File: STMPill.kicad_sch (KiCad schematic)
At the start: 65 parts, among them J1 Conn_Coaxial, J2 TC2030, J3 USB_C_16P, J4 Conn_01x20_L, J5 Conn_01x20_R, Q1 SS8550, Q3 SS8050, SW1 SW_Push, SW2 SW_Push, U1 STM32WB55REVx, U2 CP2102N-Axx-xQFN24, U3 TPS78233DDC, U4 USBLC6-2SC6, X1 32MHz, Y1 32.768kHz

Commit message: saving
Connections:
- net +3.3V: now also J4.2 (Pin_2)
- net GND: now also J4.4 (Pin_4); no longer J4.2 (Pin_2)
- net PB5: no longer J4.7 (Pin_7)
- net PB7: now also J4.7 (Pin_7)
- net PC12: no longer J4.4 (Pin_4)
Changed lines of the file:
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@@
 	(wire
 		(pts
+			(xy 33.02 198.12) (xy 38.1 198.12)
+		)
+		(stroke
+			(width 0)
+			(type default)
+		)
+	)
+	(wire
+		(pts
 			(xy 368.3 129.54) (xy 368.3 127)
 		)
@@
 		)
 	)
-	(label "PC12"
-		(at 38.1 198.12 180)
-		(effects
-			(font
-				(size 1.27 1.27)
-			)
-			(justify right bottom)
-		)
-	)
 	(label "PA11"
 		(at 69.85 205.74 180)
@@
 		)
 	)
-	(label "PB5"
+	(label "PB7"
 		(at 38.1 205.74 180)
 		(effects
@@
 	)
 	(symbol
+		(lib_id "power:+3.3V")
+		(at 33.02 193.04 90)
+		(unit 1)
+		(body_style 1)
+		(exclude_from_sim no)
+		(in_bom yes)
+		(on_board yes)
+		(in_pos_files yes)
+		(dnp no)
+		(fields_autoplaced yes)
+		(property "Reference" "#PWR036"
+			(at 36.83 193.04 0)
+			(hide yes)
+			(show_name no)
+			(do_not_autoplace no)
+			(effects
+				(font
+					(size 1.27 1.27)
+				)
+			)
+		)
+		(property "Value" "+3.3V"
+			(at 29.21 193.0399 90)
+			(show_name no)
+			(do_not_autoplace no)
+			(effects
+				(font
+					(size 1.27 1.27)
+				)
+				(justify left)
+			)
+		)
+		(property "Footprint" ""
+			(at 33.02 193.04 0)
+			(hide yes)
+			(show_name no)
+			(do_not_autoplace no)
+			(effects
+				(font
+					(size 1.27 1.27)
+				)
+			)
+		)
+		(property "Datasheet" ""
+			(at 33.02 193.04 0)
+			(hide yes)
+			(show_name no)
+			(do_not_autoplace no)
+			(effects
+				(font
+					(size 1.27 1.27)
+				)
+			)
+		)
+		(property "Description" "Power symbol creates a global label with name \"+3.3V\""
+			(at 33.02 193.04 0)
+			(hide yes)
+			(show_name no)
+			(do_not_autoplace no)
+			(effects
+				(font
+					(size 1.27 1.27)
+				)
+			)
+		)
+		(pin "1"
+		)
+		(instances
+			(project "STMPill"
+				(path "/456d5bce-2783-4e9b-b1a6-9e254196200d"
+					(reference "#PWR036")
+					(unit 1)
+				)
+			)
+		)
+	)
+	(symbol
 		(lib_id "Connector_Generic:Conn_01x20")
 		(at 74.93 213.36 0)
@@
 	)
 	(symbol
+		(lib_id "power:GND")
+		(at 33.02 198.12 270)
+		(unit 1)
+		(body_style 1)
+		(exclude_from_sim no)
+		(in_bom yes)
+		(on_board yes)
+		(in_pos_files yes)
+		(dnp no)
+		(fields_autoplaced yes)
+		(property "Reference" "#PWR037"
+			(at 26.67 198.12 0)
+			(hide yes)
+			(show_name no)
+			(do_not_autoplace no)
+			(effects
+				(font
+					(size 1.27 1.27)
+				)
+			)
+		)
+		(property "Value" "GND"
+			(at 27.94 198.12 0)
+			(hide yes)
+			(show_name no)
+			(do_not_autoplace no)
+			(effects
+				(font
+					(size 1.27 1.27)
+				)
+			)
+		)
+		(property "Footprint" ""
+			(at 33.02 198.12 0)
+			(hide yes)
+			(show_name no)
+			(do_not_autoplace no)
+			(effects
+				(font
+					(size 1.27 1.27)
+				)
+			)
+		)
+		(property "Datasheet" ""
+			(at 33.02 198.12 0)
+			(hide yes)
+			(show_name no)
+			(do_not_autoplace no)
+			(effects
+				(font
+					(size 1.27 1.27)
+				)
+			)
+		)
+		(property "Description" "Power symbol creates a global label with name \"GND\" , ground"
+			(at 33.02 198.12 0)
+			(hide yes)
+			(show_name no)
+			(do_not_autoplace no)
+			(effects
+				(font
+					(size 1.27 1.27)
+				)
+			)
+		)
+		(pin "1"
+		)
+		(instances
+			(project "STMPill"
+				(path "/456d5bce-2783-4e9b-b1a6-9e254196200d"
+					(reference "#PWR037")
+					(unit 1)
+				)
+			)
+		)
+	)
+	(symbol
 		(lib_id "Device:LED")
 		(at 297.18 129.54 90)
@@
 	)
 	(symbol
+		(lib_id "power:GND")
+		(at 33.02 195.58 270)
+		(unit 1)
+		(body_style 1)
+		(exclude_from_sim no)
+		(in_bom yes)
+		(on_board yes)
+		(in_pos_files yes)
+		(dnp no)
+		(fields_autoplaced yes)
+		(property "Reference" "#PWR038"
+			(at 26.67 195.58 0)
+			(hide yes)
+			(show_name no)
+			(do_not_autoplace no)
+			(effects
+				(font
+					(size 1.27 1.27)
+				)
+			)
+		)
+		(property "Value" "GND"
+			(at 27.94 195.58 0)
+			(hide yes)
+			(show_name no)
+			(do_not_autoplace no)
+			(effects
+				(font
+					(size 1.27 1.27)
+				)
+			)
+		)
+		(property "Footprint" ""
+			(at 33.02 195.58 0)
+			(hide yes)
+			(show_name no)
+			(do_not_autoplace no)
+			(effects
+				(font
+					(size 1.27 1.27)
+				)
+			)
+		)
+		(property "Datasheet" ""
+			(at 33.02 195.58 0)
+			(hide yes)
+			(show_name no)
+			(do_not_autoplace no)
+			(effects
+				(font
+					(size 1.27 1.27)
+				)
+			)
+		)
+		(property "Description" "Power symbol creates a global label with name \"GND\" , ground"
+			(at 33.02 195.58 0)
+			(hide yes)
+			(show_name no)
+			(do_not_autoplace no)
+			(effects
+				(font
+					(size 1.27 1.27)
+				)
+			)
+		)
+		(pin "1"
+		)
+		(instances
+			(project "STMPill"
+				(path "/456d5bce-2783-4e9b-b1a6-9e254196200d"
+					(reference "#PWR038")
+					(unit 1)
+				)
+			)
+		)
+	)
+	(symbol
 		(lib_id "Device:C")
 		(at 93.98 41.91 0)
@@
 	(symbol
 		(lib_id "power:GND")
-		(at 33.02 193.04 270)
-		(unit 1)
-		(body_style 1)
-		(exclude_from_sim no)
-		(in_bom yes)
-		(on_board yes)
-		(in_pos_files yes)
-		(dnp no)
-		(fields_autoplaced yes)
-		(property "Reference" "#PWR036"
-			(at 26.67 193.04 0)
-			(hide yes)
-			(show_name no)
-			(do_not_autoplace no)
-			(effects
-				(font
-					(size 1.27 1.27)
-				)
-			)
-		)
-		(property "Value" "GND"
-			(at 27.94 193.04 0)
-			(hide yes)
-			(show_name no)
-			(do_not_autoplace no)
-			(effects
-				(font
-					(size 1.27 1.27)
-				)
-			)
-		)
-		(property "Footprint" ""
-			(at 33.02 193.04 0)
-			(hide yes)
-			(show_name no)
-			(do_not_autoplace no)
-			(effects
-				(font
-					(size 1.27 1.27)
-				)
-			)
-		)
-		(property "Datasheet" ""
-			(at 33.02 193.04 0)
-			(hide yes)
-			(show_name no)
-			(do_not_autoplace no)
-			(effects
-				(font
-					(size 1.27 1.27)
-				)
-			)
-		)
-		(property "Description" "Power symbol creates a global label with name \"GND\" , ground"
-			(at 33.02 193.04 0)
-			(hide yes)
-			(show_name no)
-			(do_not_autoplace no)
-			(effects
-				(font
-					(size 1.27 1.27)
-				)
-			)
-		)
-		(pin "1"
-		)
-		(instances
-			(project "STMPill"
-				(path "/456d5bce-2783-4e9b-b1a6-9e254196200d"
-					(reference "#PWR036")
-					(unit 1)
-				)
-			)
-		)
-	)
-	(symbol
-		(lib_id "power:GND")
 		(at 58.42 193.04 270)
 		(unit 1)
@@
 					(unit 1)
 				)
-			)
-		)
-	)
-	(symbol
-		(lib_id "power:GND")
-		(at 33.02 195.58 270)
-		(unit 1)
-		(body_style 1)
-		(exclude_from_sim no)
-		(in_bom yes)
-		(on_board yes)
-		(in_pos_files yes)
-		(dnp no)
-		(fields_autoplaced yes)
-		(property "Reference" "#PWR037"
-			(at 26.67 195.58 0)
-			(hide yes)
-			(show_name no)
-			(do_not_autoplace no)
-			(effects
-				(font
-					(size 1.27 1.27)
-				)
-			)
-		)
-		(property "Value" "GND"
-			(at 27.94 195.58 0)
-			(hide yes)
-			(show_name no)
-			(do_not_autoplace no)
-			(effects
-				(font
-					(size 1.27 1.27)
-				)
-			)
-		)
-		(property "Footprint" ""
-			(at 33.02 195.58 0)
-			(hide yes)
-			(show_name no)
-			(do_not_autoplace no)
-			(effects
-				(font
-					(size 1.27 1.27)
-				)
-			)
-		)
-		(property "Datasheet" ""
-			(at 33.02 195.58 0)
-			(hide yes)
-			(show_name no)
-			(do_not_autoplace no)
-			(effects
-				(font
-					(size 1.27 1.27)
-				)
-			)
-		)
-		(property "Description" "Power symbol creates a global label with name \"GND\" , ground"
-			(at 33.02 195.58 0)
-			(hide yes)
-			(show_name no)
-			(do_not_autoplace no)
-			(effects
-				(font
-					(size 1.27 1.27)
-				)
-			)
-		)
-		(pin "1"
-		)
-		(instances
-			(project "STMPill"
-				(path "/456d5bce-2783-4e9b-b1a6-9e254196200d"
-					(reference "#PWR037")
-					(unit 1)
-				)

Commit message: touchups
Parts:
- added FID1, FID2, FID3: Fiducial, Fiducial:Fiducial_0.5mm_Mask1mm, symbol Mechanical:Fiducial
- C14: LCSC Part C1525 -> C53273
- D5: LCSC Part (none) -> C191023
- SW1, SW2: footprint jej:SW_PUSH_SMD,3x2mm -> easyeda2kicad:KEY-SMD_L3.9-W3.0-LS5.0-EH

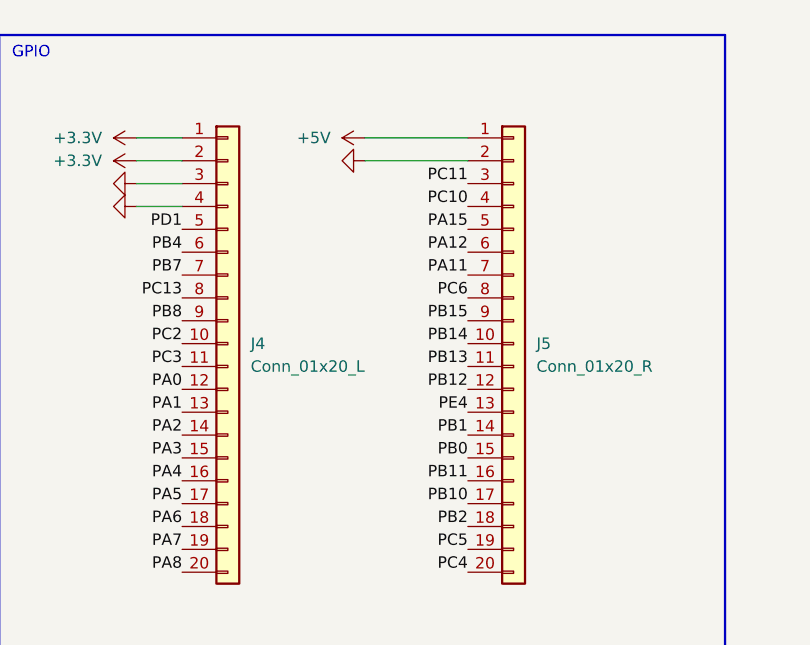
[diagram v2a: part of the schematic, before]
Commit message: fixing footprints
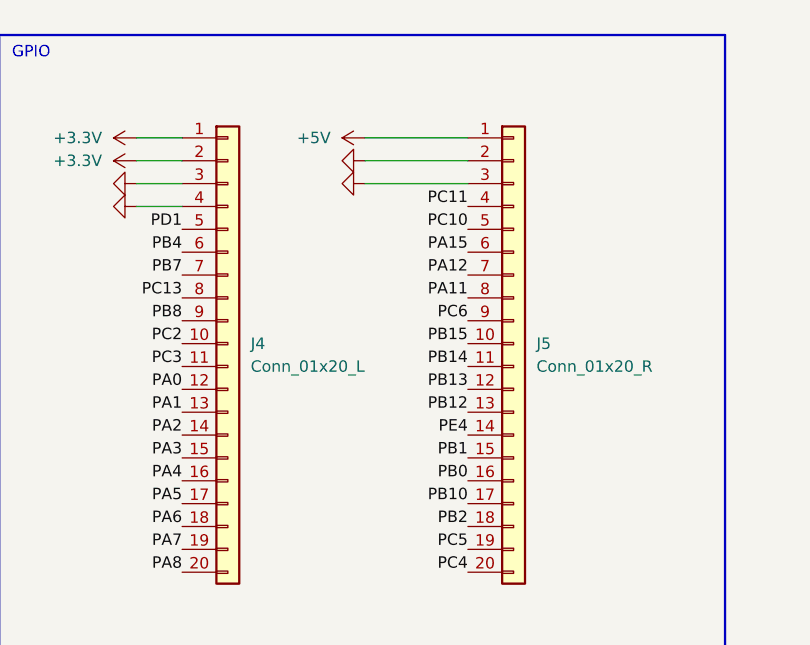
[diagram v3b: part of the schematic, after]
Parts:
- C1, C10, C11, C12, C13, C14, C15, C16, C17, C18, C19, C2, C20, C21, C22, C23, C24, C25, C3, C4, C5, C6, C7, C8, C9: footprint Capacitor_SMD:C_01005_0402Metric -> Capacitor_SMD:C_0402_1005Metric
- D1, D3, D4: footprint LED_SMD:LED_0201_0603Metric -> Diode_SMD:D_0402_1005Metric; LCSC Part C126319 -> C598352
- D2: footprint LED_SMD:LED_0201_0603Metric -> Diode_SMD:D_0402_1005Metric; LCSC Part C84269 -> C130720
- L1, L3: footprint Inductor_SMD:L_01005_0402Metric -> Inductor_SMD:L_0402_1005Metric
- R1, R10, R11, R12, R13, R2, R3, R4, R5, R6, R7, R8, R9: footprint Resistor_SMD:R_01005_0402Metric -> Resistor_SMD:R_0402_1005Metric
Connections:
- net GND: now also J5.3 (Pin_3)
- net PA11: now also J5.8 (Pin_8); no longer J5.7 (Pin_7)
- net PA12: now also J5.7 (Pin_7); no longer J5.6 (Pin_6)
- net PA15: now also J5.6 (Pin_6); no longer J5.5 (Pin_5)
- net PB0: now also J5.16 (Pin_16); no longer J5.15 (Pin_15)
- net PB1: now also J5.15 (Pin_15); no longer J5.14 (Pin_14)
- net PB11: no longer J5.16 (Pin_16)
- net PB12: now also J5.13 (Pin_13); no longer J5.12 (Pin_12)
- net PB13: now also J5.12 (Pin_12); no longer J5.11 (Pin_11)
- net PB14: now also J5.11 (Pin_11); no longer J5.10 (Pin_10)
- net PB15: now also J5.10 (Pin_10); no longer J5.9 (Pin_9)
- net PC10: now also J5.5 (Pin_5); no longer J5.4 (Pin_4)
- net PC11: now also J5.4 (Pin_4); no longer J5.3 (Pin_3)
- net PC6: now also J5.9 (Pin_9); no longer J5.8 (Pin_8)
- net PE4: now also J5.14 (Pin_14); no longer J5.13 (Pin_13)
